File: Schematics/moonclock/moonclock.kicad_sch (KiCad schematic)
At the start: 29 parts, among them J1 Conn_01x05, J2 Screw_Terminal_01x04, J3 Screw_Terminal_01x03, J4 Conn_01x04, J5 Conn_01x04, U1 RP2040-Zero, U2 MCP4922-ESL, U3 MAX6071AAUT21+T, U4 MCP6002-xSN

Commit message: Start on rev 2 design
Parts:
- added BT1: Battery_Cell, bs7:BAT_BS-7, symbol Device:Battery_Cell
- added U5: MCP7940N-xSN, Package_SO:SOIC-8_3.9x4.9mm_P1.27mm, symbol Timer_RTC:MCP7940N-xSN
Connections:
- net GND: now also BT1.2 (-)
- new net: BT1.1 (+), U5.3 (VBAT)
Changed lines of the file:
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@@
 	(wire
 		(pts
+			(xy 111.76 110.49) (xy 111.76 121.92)
+		)
+		(stroke
+			(width 0)
+			(type default)
+		)
+	)
+	(wire
+		(pts
 			(xy 152.4 114.3) (xy 152.4 106.68)
 		)
@@
 	(wire
 		(pts
+			(xy 125.73 110.49) (xy 111.76 110.49)
+		)
+		(stroke
+			(width 0)
+			(type default)
+		)
+	)
+	(wire
+		(pts
 			(xy 231.14 83.82) (xy 231.14 91.44)
 		)
@@
 	(symbol
 		(lib_id "power:GND")
+		(at 125.73 118.11 0)
+		(unit 1)
+		(exclude_from_sim no)
+		(in_bom yes)
+		(on_board yes)
+		(dnp no)
+		(fields_autoplaced yes)
+		(property "Reference" "#PWR027"
+			(at 125.73 124.46 0)
+			(effects
+				(font
+					(size 1.27 1.27)
+				)
+				(hide yes)
+			)
+		)
+		(property "Value" "GND"
+			(at 125.73 123.19 0)
+			(effects
+				(font
+					(size 1.27 1.27)
+				)
+			)
+		)
+		(property "Footprint" ""
+			(at 125.73 118.11 0)
+			(effects
+				(font
+					(size 1.27 1.27)
+				)
+				(hide yes)
+			)
+		)
+		(property "Datasheet" ""
+			(at 125.73 118.11 0)
+			(effects
+				(font
+					(size 1.27 1.27)
+				)
+				(hide yes)
+			)
+		)
+		(property "Description" "Power symbol creates a global label with name \"GND\" , ground"
+			(at 125.73 118.11 0)
+			(effects
+				(font
+					(size 1.27 1.27)
+				)
+				(hide yes)
+			)
+		)
+		(pin "1"
+		)
+		(instances
+			(project "moonclock"
+				(path "/0874c1a2-9337-4689-b98e-3f715d091ef0"
+					(reference "#PWR027")
+					(unit 1)
+				)
+			)
+		)
+	)
+	(symbol
+		(lib_id "power:GND")
 		(at 231.14 68.58 0)
 		(unit 1)
@@
 	)
 	(symbol
+		(lib_id "Device:Battery_Cell")
+		(at 125.73 115.57 0)
+		(unit 1)
+		(exclude_from_sim no)
+		(in_bom yes)
+		(on_board yes)
+		(dnp no)
+		(fields_autoplaced yes)
+		(property "Reference" "BT1"
+			(at 129.54 112.4584 0)
+			(effects
+				(font
+					(size 1.27 1.27)
+				)
+				(justify left)
+			)
+		)
+		(property "Value" "Battery_Cell"
+			(at 129.54 114.9984 0)
+			(effects
+				(font
+					(size 1.27 1.27)
+				)
+				(justify left)
+			)
+		)
+		(property "Footprint" "bs7:BAT_BS-7"
+			(at 125.73 114.046 90)
+			(effects
+				(font
+					(size 1.27 1.27)
+				)
+				(hide yes)
+			)
+		)
+		(property "Datasheet" "~"
+			(at 125.73 114.046 90)
+			(effects
+				(font
+					(size 1.27 1.27)
+				)
+				(hide yes)
+			)
+		)
+		(property "Description" "Single-cell battery"
+			(at 125.73 115.57 0)
+			(effects
+				(font
+					(size 1.27 1.27)
+				)
+				(hide yes)
+			)
+		)
+		(pin "2"
+		)
+		(pin "1"
+		)
+		(instances
+			(project ""
+				(path "/0874c1a2-9337-4689-b98e-3f715d091ef0"
+					(reference "BT1")
+					(unit 1)
+				)
+			)
+		)
+	)
+	(symbol
 		(lib_id "power:+3.3V")
 		(at 78.74 53.34 0)
@@
 					(unit 1)
 				)
+			)
+		)
+	)
+	(symbol
+		(lib_id "Timer_RTC:MCP7940N-xSN")
+		(at 109.22 132.08 0)
+		(unit 1)
+		(exclude_from_sim no)
+		(in_bom yes)
+		(on_board yes)
+		(dnp no)
+		(fields_autoplaced yes)
+		(property "Reference" "U5"
+			(at 111.3633 142.24 0)
+			(effects
+				(font
+					(size 1.27 1.27)
+				)
+				(justify left)
+			)
+		)
+		(property "Value" "MCP7940N-xSN"
+			(at 111.3633 144.78 0)
+			(effects
+				(font
+					(size 1.27 1.27)
+				)
+				(justify left)
+			)
+		)
+		(property "Footprint" "Package_SO:SOIC-8_3.9x4.9mm_P1.27mm"
+			(at 109.22 132.08 0)
+			(effects
+				(font
+					(size 1.27 1.27)
+				)
+				(hide yes)
+			)
+		)
+		(property "Datasheet" "http://ww1.microchip.com/downloads/en/DeviceDoc/20005010F.pdf"
+			(at 109.22 132.08 0)
+			(effects
+				(font
+					(size 1.27 1.27)
+				)
+				(hide yes)
+			)
+		)
+		(property "Description" "Real-Time Clock, I2C, Battery Backup, SOIC-8"
+			(at 109.22 132.08 0)
+			(effects
+				(font
+					(size 1.27 1.27)
+				)
+				(hide yes)
+			)
+		)
+		(pin "4"
+		)
+		(pin "6"
+		)
+		(pin "5"
+		)
+		(pin "1"
+		)
+		(pin "7"
+		)
+		(pin "8"
+		)
+		(pin "2"
+		)
+		(pin "3"
+		)
+		(instances
+			(project ""
+				(path "/0874c1a2-9337-4689-b98e-3f715d091ef0"
+					(reference "U5")
+					(unit 1)
+				)

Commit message: Finished Rev2 pre-gerber
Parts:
- removed J3: Screw_Terminal_01x03, TerminalBlock_RND:TerminalBlock_RND_205-00233_1x03_P5.08mm_Horizontal, symbol Connector:Screw_Terminal_01x03
- removed R10, R11: 10k, Resistor_SMD:R_0805_2012Metric_Pad1.20x1.40mm_HandSolder, symbol Device:R_US
- removed U2: MCP4922-ESL, Package_SO:SO-14_3.9x8.65mm_P1.27mm, symbol Analog_DAC:MCP4922-ESL
- removed U3: MAX6071AAUT21+T, Package_TO_SOT_SMD:SOT-23-6, symbol Reference_Voltage:MAX6071AAUT21+T
- added C4: 100n, Capacitor_SMD:C_0805_2012Metric_Pad1.18x1.45mm_HandSolder, symbol Device:C_US
- added J1: Conn_01x06, Connector_PinHeader_2.54mm:PinHeader_1x06_P2.54mm_Vertical, symbol Connector_Generic:Conn_01x06
- added J3, J5: Screw_Terminal_01x04, TerminalBlock_Phoenix:TerminalBlock_Phoenix_MKDS-1,5-4-5.08_1x04_P5.08mm_Horizontal, symbol Connector:Screw_Terminal_01x04
- added U3: MCP47FVB22-E/ST, Package_SO:TSSOP-8_4.4x3mm_P0.65mm, symbol MCP47FVB22:MCP47FVB22
- added Y1: ECS-.327-6-17X-C-TR, moonclock:XTAL_ECS-.327-6-17X-C-TR, symbol ECS-XTAL-moonclock:ECS-.327-6-17X-C-TR
- BT1: value Battery_Cell -> CR2032; footprint bs7:BAT_BS-7 -> moonclock:BAT_BS-7
- C2, C3: value 100n -> 6p; footprint Capacitor_SMD:C_0805_2012Metric_Pad1.18x1.45mm_HandSolder -> Capacitor_SMD:C_0603_1608Metric_Pad1.08x0.95mm_HandSolder
- J4: renamed from J2; footprint TerminalBlock_RND:TerminalBlock_RND_205-00234_1x04_P5.08mm_Horizontal -> TerminalBlock_Phoenix:TerminalBlock_Phoenix_MKDS-1,5-4-5.08_1x04_P5.08mm_Horizontal
- renumbered C4 to C5, J5 to J2, J4 to J6, J1 to J7, JP2 to JP1, JP1 to JP2, R5 to R10, R4 to R11, R2 to R12, R9 to R2, R7 to R3, R8 to R4, R12 to R5, R13 to R6, R14 to R7, R6 to R8, R3 to R9, U4 to U2, U5 to U4
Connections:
- net VREF_2048 is gone; now on an unnamed net: C2.1
- net +3.3V: now also U4.8 (VCC), C4.1, J1.5 (Pin_5), U3.1 (VDD), U3.2 (VREF); no longer C3.1
- net GND: now also U4.4 (VSS), C4.2, J1.6 (Pin_6), J3.2 (Pin_2), J3.4 (Pin_4), J5.2 (Pin_2), J5.4 (Pin_4), U3.5 (VSS), U3.6 (~{LAT})
- net I2C1_SCL: now also U4.6 (SCL), U3.7 (SCL)
- net I2C1_SDA: now also U4.5 (SDA), U3.8 (SDA)
- net LEFT_BUT: now also J3.1 (Pin_1)
- net M1_DAC: now also U3.3 (VOUT0)
- net M2_DAC: now also U3.4 (VOUT1)
- net RIGHT_BUT: now also U1.8 (GP7), J3.3 (Pin_3); no longer U1.5 (GP4)
- net at U4.1 (X1): now also Y1.1
- net at U4.2 (X2): now also C3.1, Y1.4
- net DAC_CS renamed EXP2
- net EXP2: now also J1.2 (Pin_2), J5.3 (Pin_3)
- net DAC_LDAC renamed EXP1
- net EXP1: now also J1.1 (Pin_1), J5.1 (Pin_1)
- net DAC_MOSI renamed EXP3
- net EXP3: now also J1.3 (Pin_3)
- net DAC_SCK renamed EXP4
- net EXP4: now also J1.4 (Pin_4)
- no-connect marks 6 -> 9
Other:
- note added: "2"
- note added: "ECS Inc ECS-.327-6-17X-C-TR XC2129CT-ND"
- note added: "EXP GPIO"
- note added: "EXP I2C"
- note added: "Expansion"
- note added: "Moon Clock By Tennessee Carmel-Veilleux"
- note removed: "RTC I2C"
- moved on the sheet: BT1, C1, C5, J4, JP1, JP2, R1, R10, R11, R12, R2, R3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

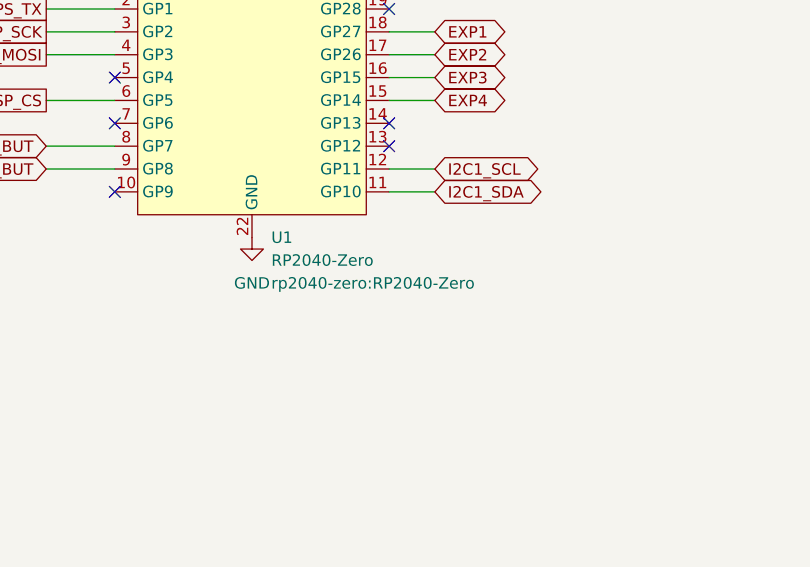
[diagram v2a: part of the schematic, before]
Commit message: Fix footprint for U1 and corner vias
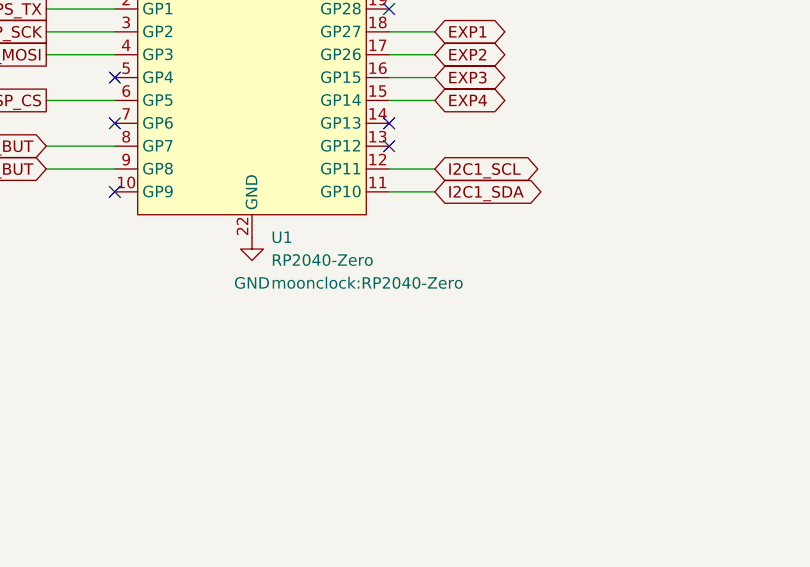
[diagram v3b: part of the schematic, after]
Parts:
- U1: footprint rp2040-zero:RP2040-Zero -> moonclock:RP2040-Zero
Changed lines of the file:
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@@
 			)
 		)
-		(property "Footprint" "rp2040-zero:RP2040-Zero"
+		(property "Footprint" "moonclock:RP2040-Zero"
 			(at 73.2633 86.36 0)
 			(effects

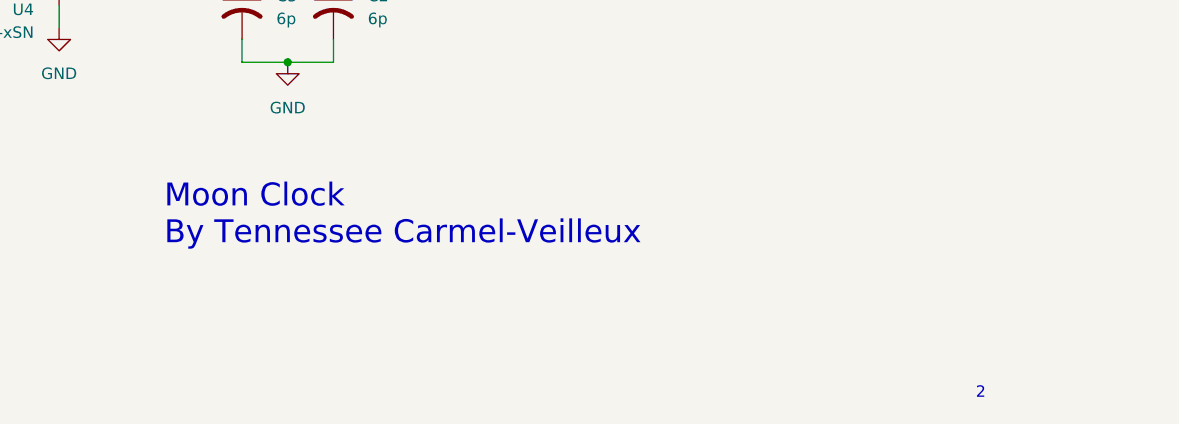
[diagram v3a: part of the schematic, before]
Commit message: Add title block to schematic and update rp2040 library location
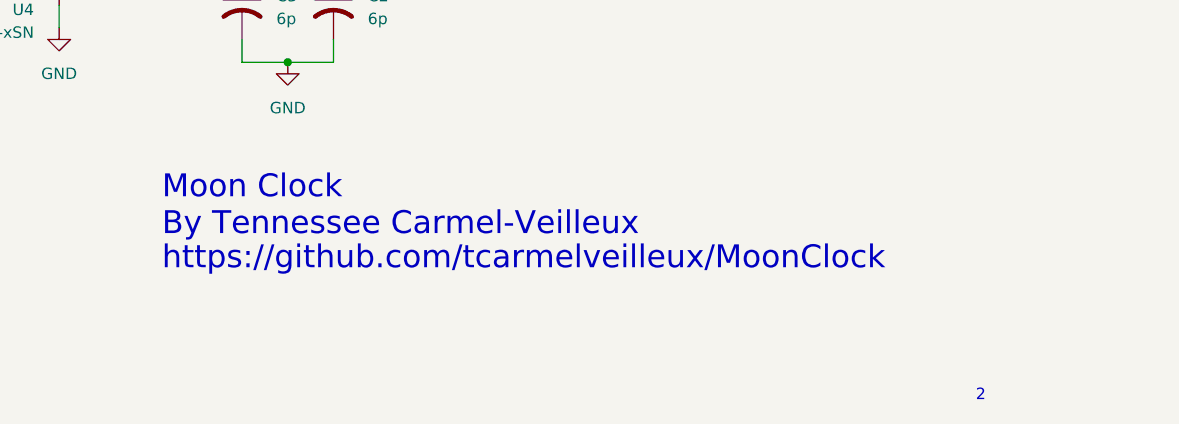
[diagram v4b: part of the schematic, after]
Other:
- note added: "https://github.com/tcarmelveilleux/MoonClock"
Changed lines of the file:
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@@
 	(generator_version "9.0")
 	(paper "A4")
+	(text "https://github.com/tcarmelveilleux/MoonClock"
+		(exclude_from_sim no)
+		(at 179.07 178.054 0)
+		(effects
+			(font
+				(size 2.54 2.54)
+			)
+			(justify left)
+			(href "https://github.com/tcarmelveilleux/MoonClock")
+		)
+	)
 	(text "Buttons"
 		(exclude_from_sim no)
@@
 	(text "2"
 		(exclude_from_sim no)
-		(at 269.494 193.04 0)
+		(at 269.494 193.294 0)
 		(effects
 			(font
@@
 	(text "Moon Clock\nBy Tennessee Carmel-Veilleux"
 		(exclude_from_sim no)
-		(at 179.324 173.228 0)
+		(at 179.07 172.212 0)
 		(effects
 			(font
